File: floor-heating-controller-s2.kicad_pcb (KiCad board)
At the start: 2 copper layers, 132 parts, among them J1 Supply, J10 VALVE1, J11 VALVE2, J12 VALVE3, J13 VALVE4, J14 VALVE5, J15 VALVE6, J16 VALVE7, J17 VALVE8, J18 Conn_01x01, J2 DS18B20_1, J3 DS18B20_2, J4 DS18B20_3, J5 DS18B20_4, J6 DS18B20_5, J7 DS18B20_6, J8 DS18B20_7, J9 DS18B20_8, U1 CJ431, U10 L9110S, U11 L9110S, U12 LM358, U13 L9110S, U14 L9110S, U2 WeMos_S2_mini, U3 LM358, U4 L9110S, U5 L9110S, U6 LM358, U7 L9110S, U8 L9110S, U9 LM358

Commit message: first placing
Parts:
- J1: footprint Connector_JST:JST_PH_B2B-PH-K_1x02_P2.00mm_Vertical -> Connector_JST:JST_PH_B2B-PH-SM4-TB_1x02-1MP_P2.00mm_Vertical
- moved R6 152.7 mm to (80.3, 140.3), turned to 180 degrees
- moved C27 152.5 mm to (85.7, 110.5)
- moved C29 152.0 mm to (80.6, 105.4), turned to -90 degrees
- moved U5 149.0 mm to (86.8, 138.4)
- moved R60 149.0 mm to (102.2, 110.5)
- moved R12 147.5 mm to (101.6, 143.5)
- moved C31 147.1 mm to (99.7, 111.8), turned to 90 degrees
- moved C7 145.7 mm to (99.1, 144.8), turned to 90 degrees
- moved R53 145.6 mm to (79.4, 108.6), turned to 180 degrees
- moved U13 144.5 mm to (85.7, 106.7)
- moved C26 144.4 mm to (99.7, 102.9), turned to 180 degrees
- moved C19 143.1 mm to (70.5, 121.3)
- moved C6 142.8 mm to (81.6, 137.2), turned to -90 degrees
- moved C2 142.6 mm to (99.7, 135.9), turned to 180 degrees
- moved C21 141.9 mm to (65.4, 116.3), turned to -90 degrees
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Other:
- board outline added: 97.8 x 66.7 mm

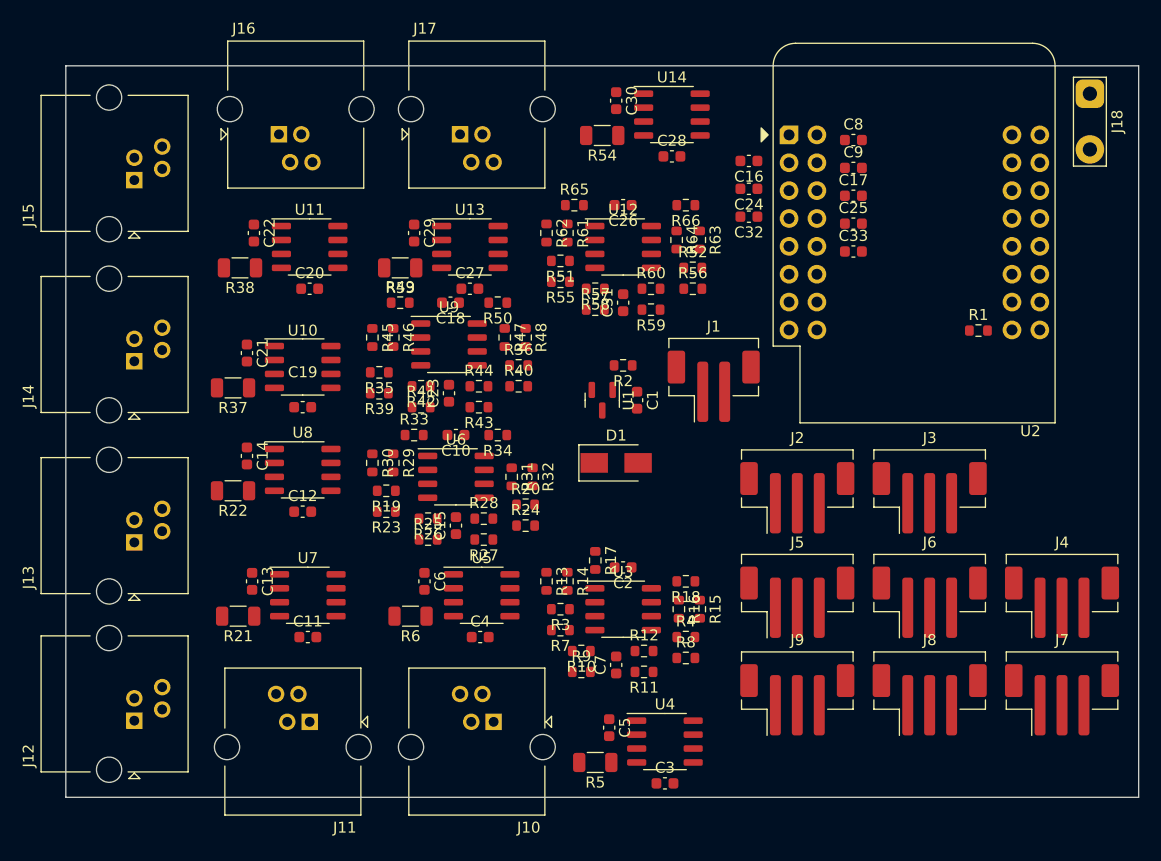
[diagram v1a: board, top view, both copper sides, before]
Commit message: First routing cycle nearly complete
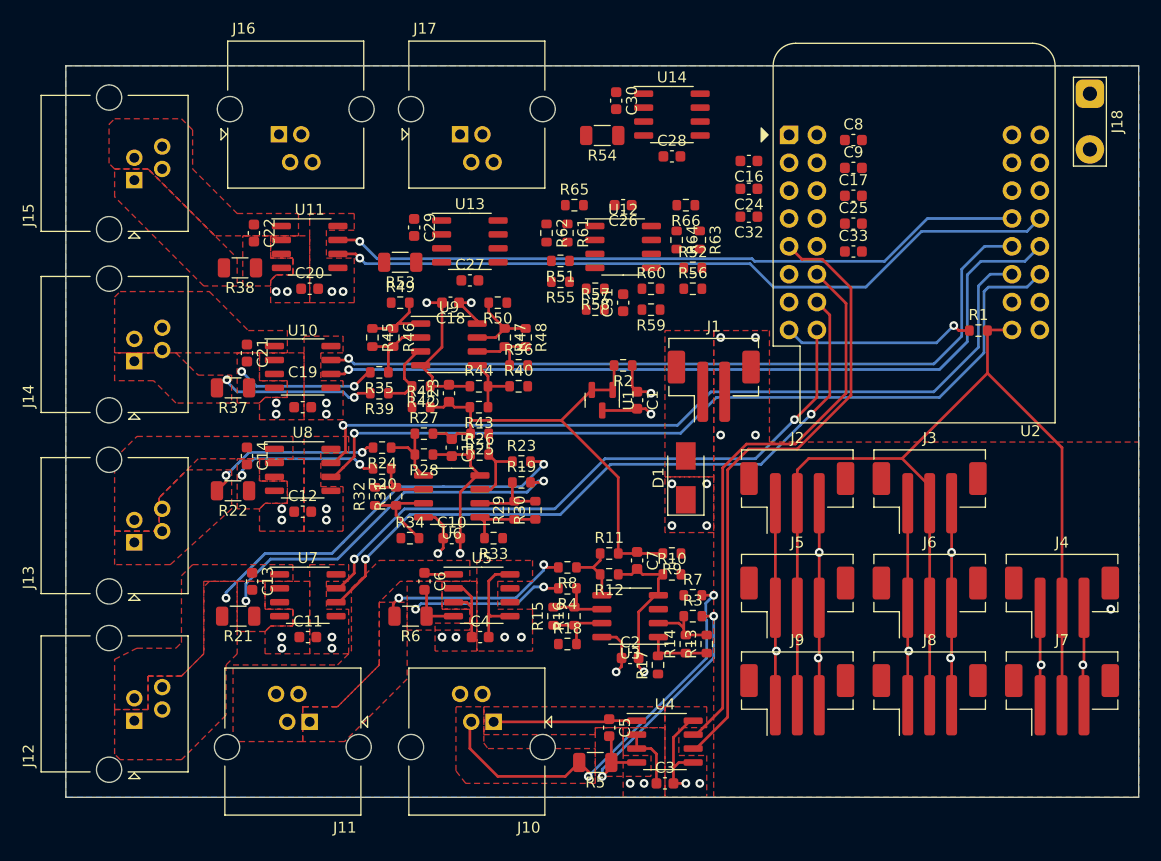
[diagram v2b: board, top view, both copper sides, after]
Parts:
- J18: value Conn_01x01 -> EXT
- moved R13 15.7 mm to (107.3, 142.9), turned to 90 degrees
- moved R30 15.5 mm to (91.7, 130.7), turned to 90 degrees
- moved R24 14.9 mm to (77.7, 125.0), turned to 180 degrees
- moved R32 14.5 mm to (77.1, 129.4), turned to 90 degrees
- moved R8 13.6 mm to (94.6, 135.9), turned to 180 degrees
- moved R9 13.6 mm to (104.1, 134.6), turned to 180 degrees
- moved R20 13.5 mm to (77.7, 126.9), turned to 180 degrees
- moved R15 13.4 mm to (93.3, 140.3), turned to 90 degrees
- moved R23 13.1 mm to (90.4, 126.2), turned to 0 degrees
- moved R7 12.5 mm to (106.0, 138.4), turned to 0 degrees
- moved R34 12.3 mm to (80.3, 133.2), turned to 0 degrees
- moved R19 12.3 mm to (90.4, 128.1), turned to 0 degrees
- moved R14 12.2 mm to (105.4, 142.9), turned to 90 degrees
- moved R18 12.2 mm to (94.6, 142.9), turned to 0 degrees
- moved R3 12.1 mm to (106.0, 140.3), turned to 0 degrees
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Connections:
- J11 pad 1: /motor_output_1/MOT2_A -> /motor_output_1/MOT2_B
- J11 pad 3: /motor_output_1/MOT2_B -> /motor_output_1/MOT2_A
- J12 pad 1: /motor_output_2/MOT1_A -> /motor_output_2/MOT1_B
- J12 pad 3: /motor_output_2/MOT1_B -> /motor_output_2/MOT1_A
- J13 pad 1: /motor_output_2/MOT2_A -> /motor_output_2/MOT2_B
- J13 pad 3: /motor_output_2/MOT2_B -> /motor_output_2/MOT2_A
- J14 pad 1: /motor_output_3/MOT1_A -> /motor_output_3/MOT1_B
- J14 pad 3: /motor_output_3/MOT1_B -> /motor_output_3/MOT1_A
- J15 pad 1: /motor_output_3/MOT2_A -> /motor_output_3/MOT2_B
- J15 pad 3: /motor_output_3/MOT2_B -> /motor_output_3/MOT2_A
- J16 pad 1: /motor_output_4/MOT1_A -> /motor_output_4/MOT1_B
- J16 pad 3: /motor_output_4/MOT1_B -> /motor_output_4/MOT1_A
- J2 pad MP: (no net) -> GND
- J3 pad MP: (no net) -> GND
- J4 pad MP: (no net) -> GND
- J5 pad MP: (no net) -> GND
- J6 pad MP: (no net) -> GND
- J7 pad MP: (no net) -> GND
- J8 pad MP: (no net) -> GND
- J9 pad MP: (no net) -> GND
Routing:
- net GND: track 0.00 -> 112.5 mm, vias 0 -> 26
- net /DS18B20: track 0.00 -> 105.2 mm
- net IN4_A: track 0.00 -> 76.8 mm, vias 0 -> 1
- net IN4_B: track 0.00 -> 74.2 mm, vias 0 -> 1
- net IN5_A: track 0.00 -> 73.0 mm, vias 0 -> 1
- net IN5_B: track 0.00 -> 70.4 mm, vias 0 -> 1
- net IN6_A: track 0.00 -> 67.8 mm, vias 0 -> 1
- net IN6_B: track 0.00 -> 63.9 mm, vias 0 -> 1
- net +5V: track 0.00 -> 63.3 mm, vias 0 -> 20
- net IN3_A: track 0.00 -> 62.7 mm, vias 0 -> 2
- net IN3_B: track 0.00 -> 57.9 mm, vias 0 -> 2
- net IN1_A: track 0.00 -> 57.9 mm
- net IN1_B: track 0.00 -> 51.6 mm
- net +2V5: track 0.00 -> 45.2 mm
- net /motor_output_1/MOT1_B: track 0.00 -> 38.0 mm, vias 0 -> 2
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- added copper zone on B.Cu, net +3V3
- added copper zone on F.Cu, net +5V
- added copper zone on In1.Cu, net +5V
- added copper zone on F.Cu, net /motor_output_1/MOT1_A
- added copper zone on F.Cu, net /motor_output_1/MOT1_B
- added copper zone on F.Cu, net /motor_output_1/MOT2_A
- added copper zone on F.Cu, net /motor_output_1/MOT2_B
- added copper zone on F.Cu, net /motor_output_2/MOT1_A
- added copper zone on F.Cu, net /motor_output_2/MOT1_B
- added copper zone on F.Cu, net /motor_output_2/MOT2_A
- added copper zone on F.Cu, net /motor_output_2/MOT2_B
- added copper zone on F.Cu, net /motor_output_3/MOT1_A
- added copper zone on F.Cu, net /motor_output_3/MOT1_B
- added copper zone on F.Cu, net /motor_output_3/MOT2_A
- added copper zone on F.Cu, net /motor_output_3/MOT2_B
- added copper zone on F.Cu, net GND
- added copper zone on In2.Cu, net GND
- added copper zone on F.Cu, net Net-(C13-Pad2)
- added copper zone on F.Cu, net Net-(C14-Pad2)
- added copper zone on F.Cu, net Net-(C21-Pad2)
- added copper zone on F.Cu, net Net-(C22-Pad2)
- added copper zone on F.Cu, net Net-(C5-Pad2)
- added copper zone on F.Cu, net Net-(C6-Pad2)
- added copper zone on F.Cu, net Net-(D1-Pad2)
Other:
- copper layers 2 -> 4

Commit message: production ready
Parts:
- added REF**: OSHW-Logo2_7.3x6mm_Copper, Symbol:OSHW-Logo2_7.3x6mm_Copper, F.Cu at (136.3, 130.9)
- moved J8 0.90 mm to (127.5, 148.9)
- moved J7 0.89 mm to (139.7, 148.8)
- moved J9 0.89 mm to (115.6, 148.8)
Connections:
- J1 pad MP: (no net) -> GND
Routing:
- net CUR2: track 0.00 -> 85.6 mm, vias 0 -> 2
- net CUR4: track 0.00 -> 79.5 mm, vias 0 -> 2
- net CUR3: track 0.00 -> 79.5 mm, vias 0 -> 2
- net CUR1: track 0.00 -> 76.6 mm, vias 0 -> 2
- net CUR5: track 0.00 -> 58.2 mm, vias 0 -> 1
- net IN7_A: track 0.00 -> 51.6 mm, vias 0 -> 1
- net CUR6: track 0.00 -> 51.3 mm, vias 0 -> 2
- net IN7_B: track 0.00 -> 50.3 mm, vias 0 -> 1
- net IN2_A: track 0.00 -> 47.2 mm, vias 0 -> 2
- net IN2_B: track 0.00 -> 43.8 mm, vias 0 -> 2
- net /motor_output_3/MOT2_B: track 0.00 -> 38.3 mm, vias 0 -> 2
- net Net-(C22-Pad2): track 0.00 -> 34.1 mm, vias 0 -> 2
- net IN8_A: track 0.00 -> 33.4 mm
- net IN8_B: track 0.00 -> 30.5 mm
- net CUR7: track 0.00 -> 23.5 mm
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- added copper zone on F.Cu, net /motor_output_4/MOT1_A
- added copper zone on F.Cu, net /motor_output_4/MOT1_B
- added copper zone on F.Cu, net /motor_output_4/MOT2_A
- added copper zone on F.Cu, net /motor_output_4/MOT2_B
- added copper zone on F.Cu, net Net-(C29-Pad2)
- added copper zone on F.Cu, net Net-(C30-Pad2)
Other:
- board text added: "floor heating controller S2 Tecnologic 2022 Rev 1"
